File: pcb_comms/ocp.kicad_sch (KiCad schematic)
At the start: 11 parts, among them Q1 SSM6K403TU_LF, U4 DTC144EET1G, U5 LTC4361HTS8-2-TRMPBF

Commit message: Last update
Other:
- company: (none) -> Sanie Peralta, Alejandro Campo
- title: (none) -> PC1: APRS & GPS
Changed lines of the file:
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@@
 	(generator_version "9.0")
 	(paper "A4")
+	(title_block
+		(title "PC1: APRS & GPS")
+		(date "2026-04-01")
+		(rev "1.0")
+		(company "Sanie Peralta, Alejandro Campo")
+		(comment 1 "Introducción a la Ingeniería Satelital ")
+		(comment 2 "Primer Parcial")
+	)
 	(text "OCP\n"
 		(exclude_from_sim no)

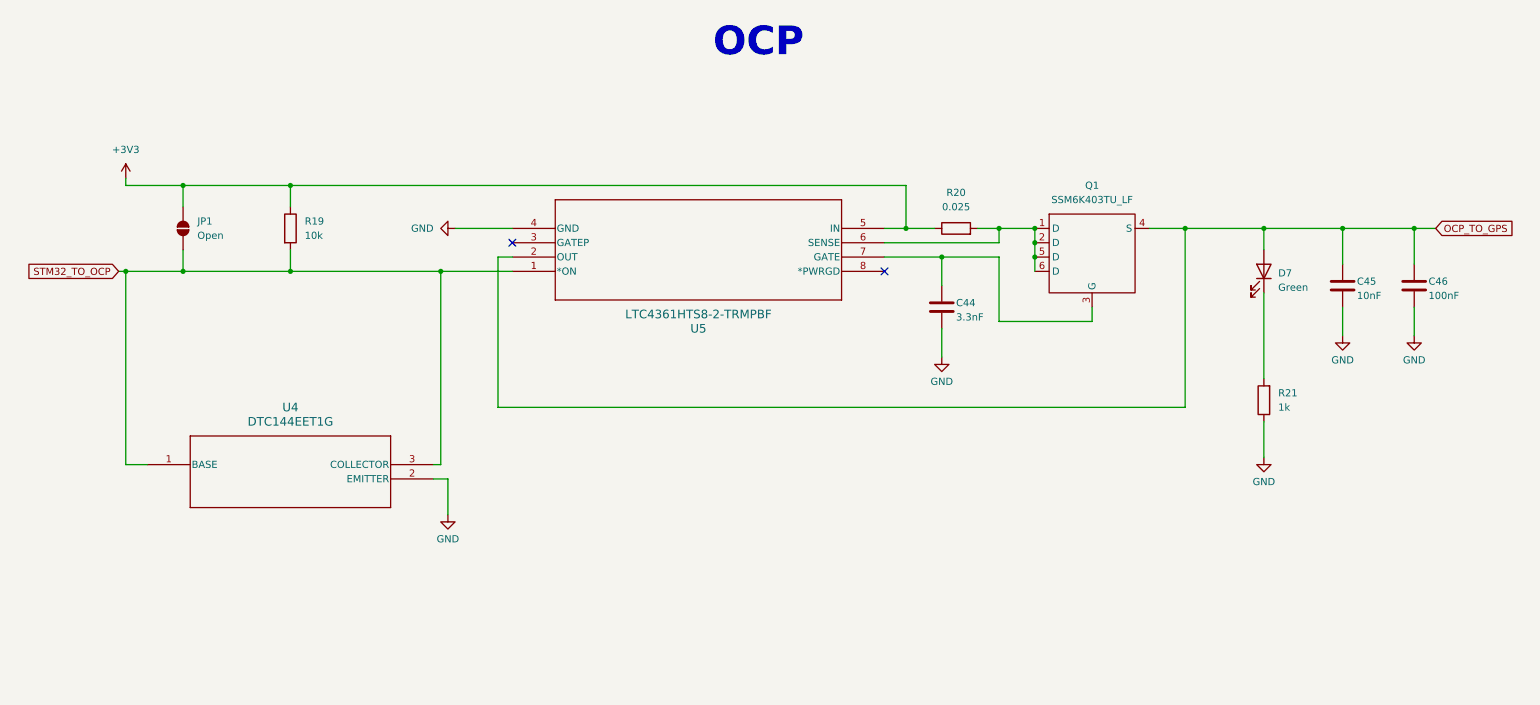
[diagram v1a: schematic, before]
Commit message: Finish schematic
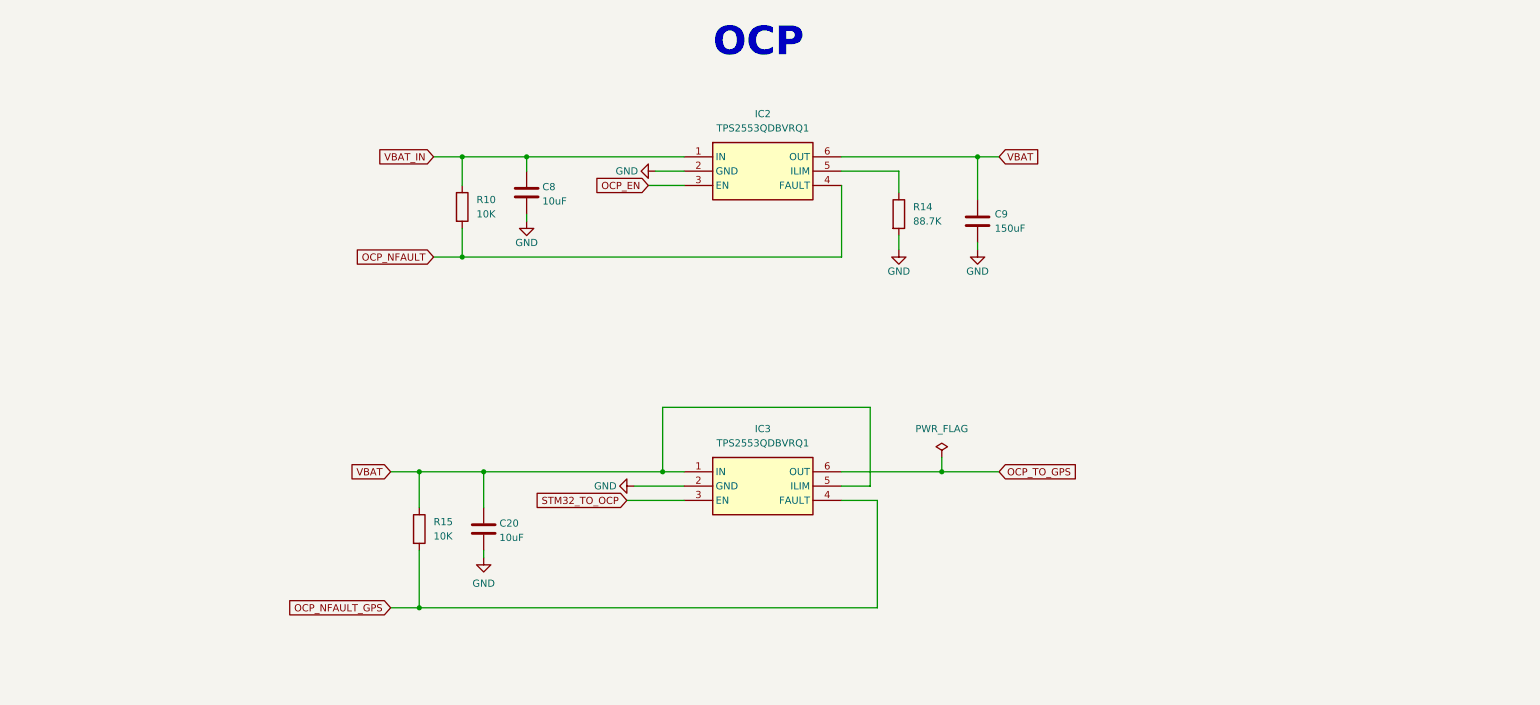
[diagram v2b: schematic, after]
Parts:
- removed C44: 3.3nF, symbol Device:C
- removed C45: 10nF, symbol Device:C
- removed C46: 100nF, symbol Device:C
- removed D7: Green, symbol Device:LED
- removed JP1: Open, symbol Jumper:SolderJumper_2_Open
- removed Q1: SSM6K403TU_LF, SSM6K403TU_LF:UF6_TOS-L, symbol OCP_SSM6K403TU_LF:SSM6K403TU_LF
- removed R19: 10k, symbol Device:R
- removed R20: 0.025, symbol Device:R
- removed R21: 1k, Resistor_SMD:R_0805_2012Metric, symbol Device:R
- removed U4: DTC144EET1G, symbol OCP_DTC144EET1G:DTC144EET1G
- removed U5: LTC4361HTS8-2-TRMPBF, symbol OCP_LTC4361HTS8_2_TRMPBF:LTC4361HTS8-2-TRMPBF
- added C20, C8: 10uF, symbol Device:C
- added C9: 150uF, symbol Device:C
- added IC2, IC3: TPS2553QDBVRQ1, symbol OCP_TPS2553QDBVRQ1:TPS2553QDBVRQ1
- added R10, R15: 10K, symbol Device:R
- added R14: 88.7K, symbol Device:R
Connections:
- net GND: now also C20.2, C8.2, C9.2, IC2.2 (GND), IC3.2 (GND), R14.2
- net OCP_TO_GPS: now also IC3.6 (OUT)
- net STM32_TO_OCP: now also IC3.3 (EN)
- new net: IC2.5 (ILIM), R14.1
- new net OCP_EN: IC2.3 (EN)
- new net OCP_NFAULT: IC2.4 (FAULT), R10.2
- new net OCP_NFAULT_GPS: IC3.4 (FAULT), R15.2
- new net VBAT: C20.1, C9.1, IC2.6 (OUT), IC3.1 (IN), IC3.5 (ILIM), R15.1
- new net VBAT_IN: C8.1, IC2.1 (IN), R10.1
- no-connect marks 2 -> 0

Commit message: Version 1.0. No DRA yet
From now on I will make the connections for IIS and then adapt it for the club
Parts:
- added C36: 150uF, symbol Device:C
- added D7: GREEN, symbol Device:LED
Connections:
- net GND: now also C36.2, D7.1 (K)
- net OCP_TO_GPS: now also C36.1
- net VBAT: now also D7.2 (A)

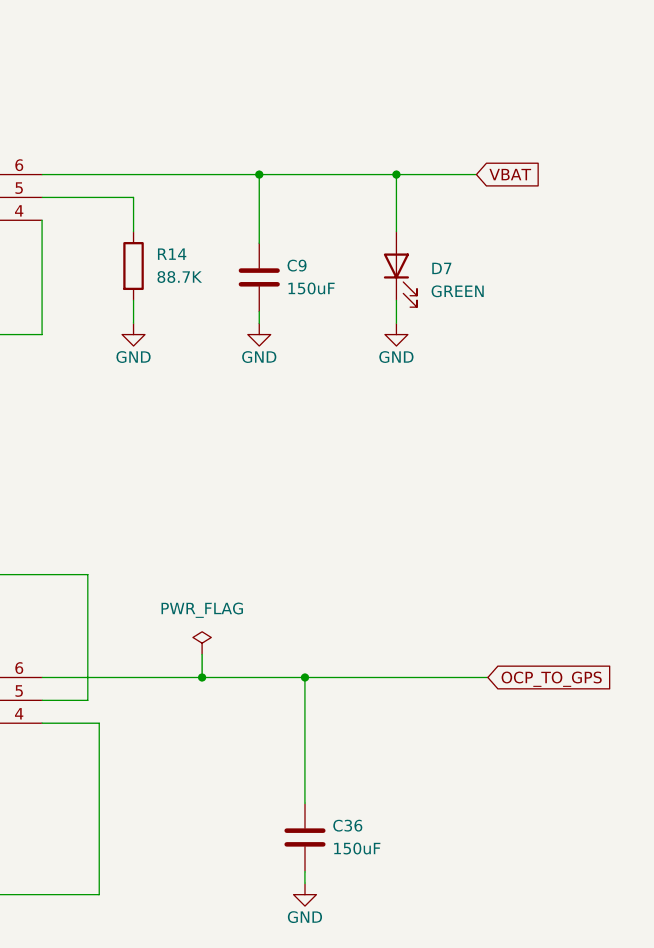
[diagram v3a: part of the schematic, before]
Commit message: Add footprints
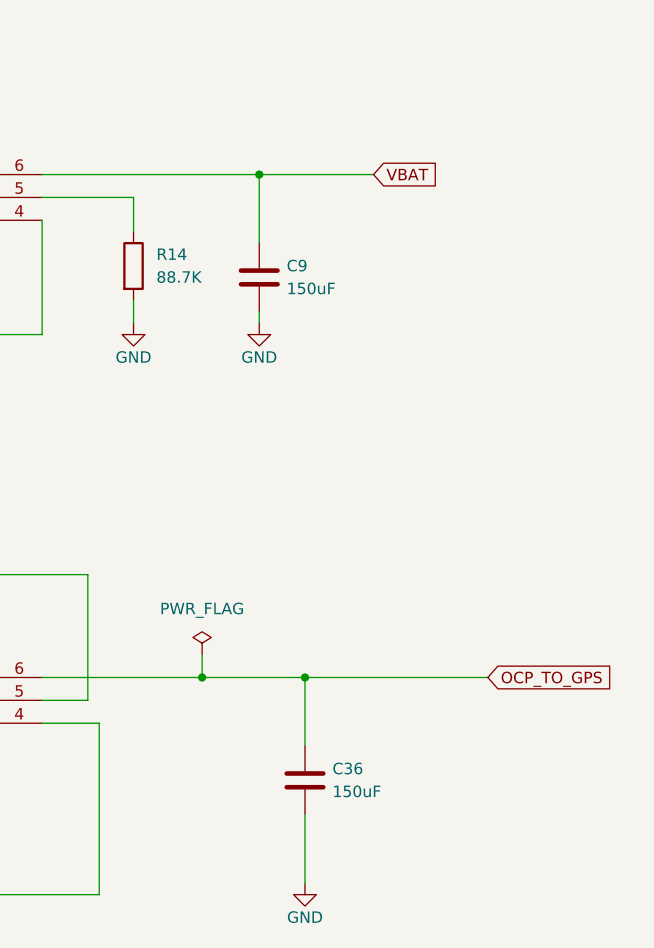
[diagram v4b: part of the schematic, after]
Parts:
- removed D7: GREEN, symbol Device:LED
- C20, C8: footprint (none) -> Capacitor_SMD:C_0805_2012Metric_Pad1.18x1.45mm_HandSolder
- C36, C9: footprint (none) -> Capacitor_SMD:C_1210_3225Metric_Pad1.33x2.70mm_HandSolder
- IC2, IC3: footprint (none) -> OCP_TPS2553QDBVRQ1:SOT95P280X145-6N
- R10, R14, R15: footprint (none) -> Resistor_SMD:R_0805_2012Metric_Pad1.20x1.40mm_HandSolder
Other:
- moved on the sheet: C36

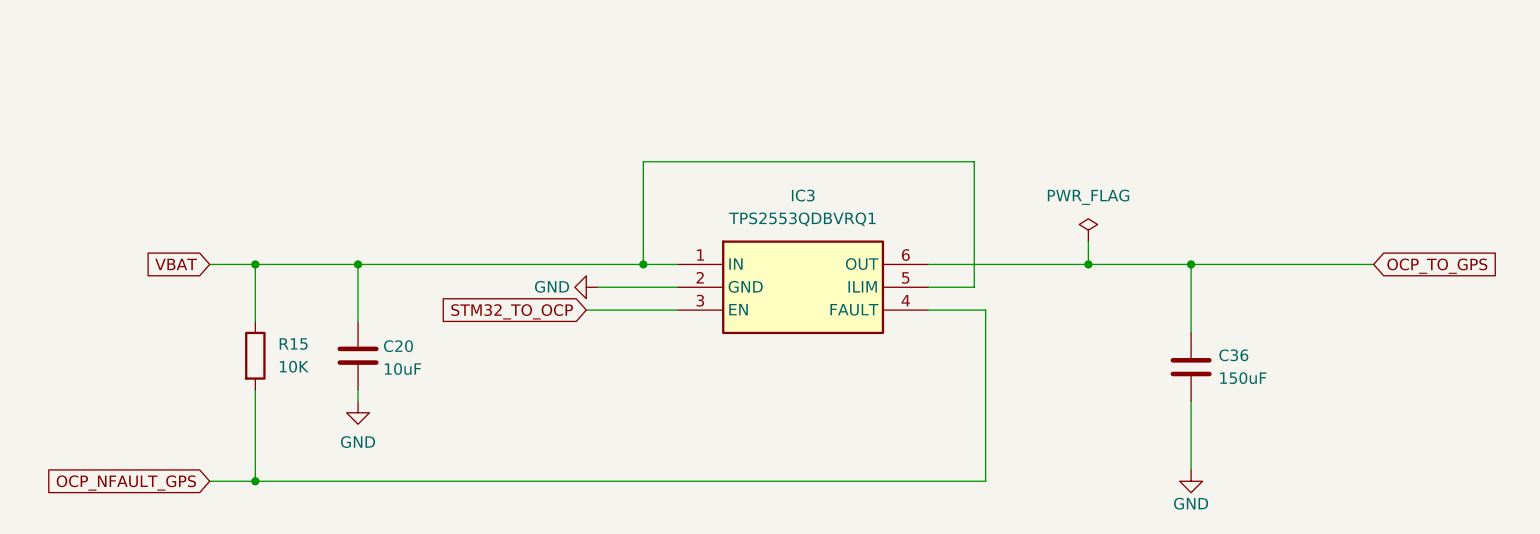
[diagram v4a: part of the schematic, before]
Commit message: remove gps
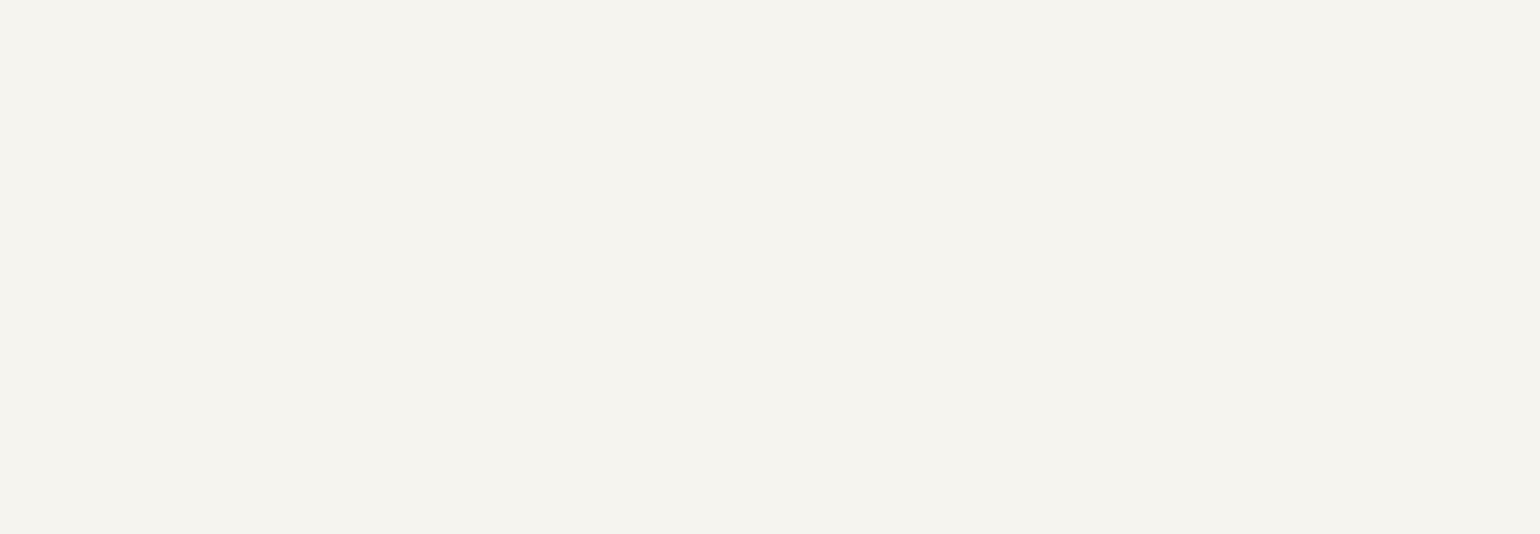
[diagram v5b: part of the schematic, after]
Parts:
- removed C20: 10uF, Capacitor_SMD:C_0805_2012Metric_Pad1.18x1.45mm_HandSolder, symbol Device:C
- removed C36: 150uF, Capacitor_SMD:C_1210_3225Metric_Pad1.33x2.70mm_HandSolder, symbol Device:C
- removed IC3: TPS2553QDBVRQ1, OCP_TPS2553QDBVRQ1:SOT95P280X145-6N, symbol OCP_TPS2553QDBVRQ1:TPS2553QDBVRQ1
- removed R15: 10K, Resistor_SMD:R_0805_2012Metric_Pad1.20x1.40mm_HandSolder, symbol Device:R

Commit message: Update DRA
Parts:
- R14: value 88.7K -> 26.1K
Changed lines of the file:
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@@
 			)
 		)
-		(property "Value" "88.7K"
+		(property "Value" "26.1K"
 			(at 172.72 69.8499 0)
 			(effects

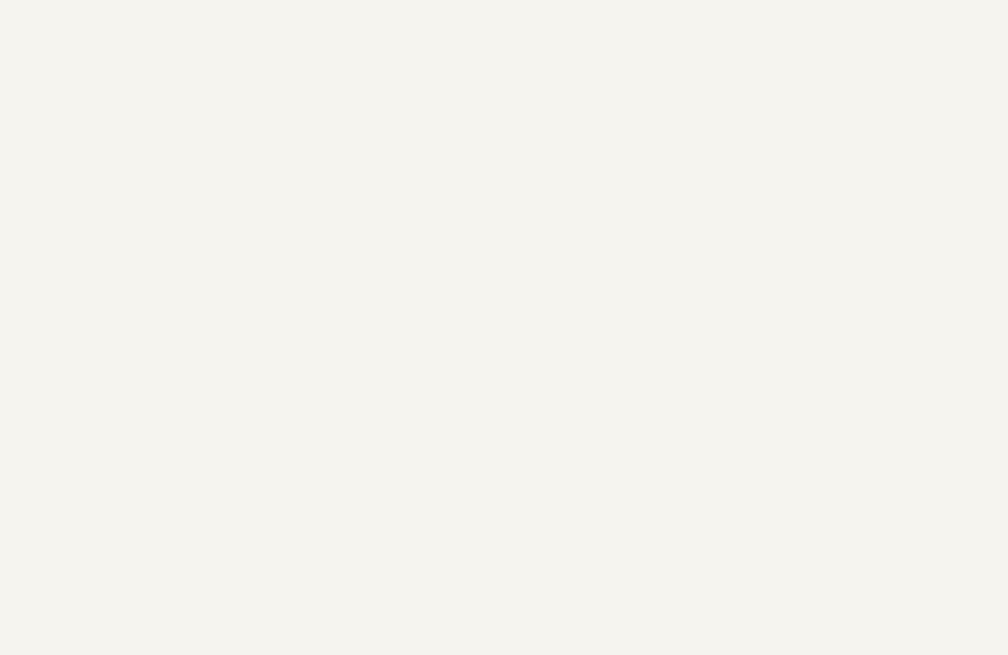
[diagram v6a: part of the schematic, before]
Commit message: Add UART USB
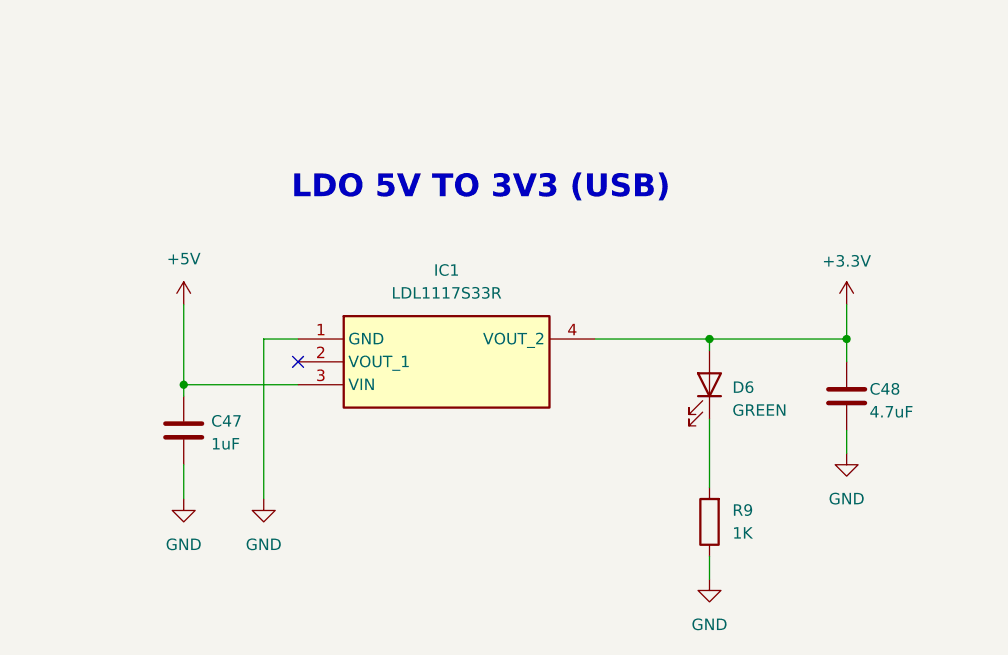
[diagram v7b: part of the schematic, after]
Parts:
- added C47: 1uF, Capacitor_SMD:C_0805_2012Metric_Pad1.18x1.45mm_HandSolder, symbol Device:C
- added C48: 4.7uF, Capacitor_SMD:C_0805_2012Metric_Pad1.18x1.45mm_HandSolder, symbol Device:C
- added D6: GREEN, LED_SMD:LED_0805_2012Metric_Pad1.15x1.40mm_HandSolder, symbol Device:LED
- added IC1: LDL1117S33R, LDO_LDL1117S33R:LDO_LDL1117S33R, symbol LDO_LDL1117S33R:LDL1117S33R
- added R9: 1K, Resistor_SMD:R_0805_2012Metric_Pad1.20x1.40mm_HandSolder, symbol Device:R
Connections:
- net GND: now also C47.2, C48.2, IC1.1 (GND), R9.1
- new net: D6.1 (K), R9.2
- new net +3.3V: C48.1, D6.2 (A), IC1.4 (VOUT_2)
- new net +5V: C47.1, IC1.3 (VIN)
- no-connect marks 0 -> 1
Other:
- note added: "LDO 5V TO 3V3 (USB)"
